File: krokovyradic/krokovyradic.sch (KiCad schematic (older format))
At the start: 1 part

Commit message: uprava
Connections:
- net labels added: +6V
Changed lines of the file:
@@
 LIBS:contrib
 LIBS:valves
+LIBS:krokovyradic-cache
 EELAYER 25 0
 EELAYER END
@@
 	1    0    0    -1
 $EndComp
+$Comp
+L +6V #PWR?
+U 1 1 5BD98FBB
+P 8000 3200
+F 0 "#PWR?" H 8000 3050 50  0001 C CNN
+F 1 "+6V" H 8000 3340 50  0000 C CNN
+F 2 "" H 8000 3200 50  0000 C CNN
+F 3 "" H 8000 3200 50  0000 C CNN
+	1    8000 3200
+	1    0    0    -1
+$EndComp

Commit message: arduino
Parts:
- removed IC?: ATMEGA328-A, TQFP32, symbol ATMEGA328-A
- added IC?: ATMEGA328-P, DIL28, symbol ATMEGA328-P
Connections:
- net labels removed: +6V
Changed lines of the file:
@@
 $EndDescr
 $Comp
-L ATMEGA328-A IC?
-U 1 1 5BD9900C
-P 5450 3600
-F 0 "IC?" H 4700 4850 50  0000 L BNN
-F 1 "ATMEGA328-A" H 5850 2200 50  0000 L BNN
-F 2 "TQFP32" H 5450 3600 50  0000 C CIN
-F 3 "" H 5450 3600 50  0000 C CNN
-	1    5450 3600
+L ATMEGA328-P IC?
+U 1 1 5BE2CED1
+P 4650 3400
+F 0 "IC?" H 3900 4650 50  0000 L BNN
+F 1 "ATMEGA328-P" H 5050 2000 50  0000 L BNN
+F 2 "DIL28" H 4650 3400 50  0000 C CIN
+F 3 "" H 4650 3400 50  0000 C CNN
+	1    4650 3400
 	1    0    0    -1
 $EndComp
-$Comp
-L +6V #PWR?
-U 1 1 5BD98FBB
-P 8000 3200
-F 0 "#PWR?" H 8000 3050 50  0001 C CNN
-F 1 "+6V" H 8000 3340 50  0000 C CNN
-F 2 "" H 8000 3200 50  0000 C CNN
-F 3 "" H 8000 3200 50  0000 C CNN
-	1    8000 3200
-	1    0    0    -1
-$EndComp

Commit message: uprava zapojeni
pridani soucastek
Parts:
- added A?: Pololu_Breakout_A4988, Module:Pololu_Breakout-16_15.2x20.3mm, symbol Driver_Motor:Pololu_Breakout_A4988
- added C?: C, symbol Device:C
- added M?: Stepper_Motor_bipolar, symbol Motor:Stepper_Motor_bipolar
- IC?: symbol ATMEGA328-P -> krokovyradic-rescue:ATMEGA328-P
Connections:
- net at IC?.22 (GND): now also A?.1 (GND)
- net at IC?.26 ((PCINT11/ADC3)PC3): now also A?.16 (DIR)
- net at IC?.27 ((PCINT12/SDA/ADC4)PC4): now also A?.15 (STEP)
- net at IC?.7 (VCC): now also A?.2 (VDD)
- new net: A?.13 (~RESET), A?.14 (~SLEEP)
- new net: A?.3 (1B), M?.2 (-)
- new net: A?.4 (1A), M?.1
- new net: A?.5 (2A), M?.3
- new net: A?.6 (2B), M?.4
- new net: A?.8 (VMOT), C?.1
- new net +7.5V: A?.7 (GND), C?.2
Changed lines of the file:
@@
-EESchema Schematic File Version 2
-LIBS:power
-LIBS:device
-LIBS:transistors
-LIBS:conn
-LIBS:linear
-LIBS:regul
-LIBS:74xx
-LIBS:cmos4000
-LIBS:adc-dac
-LIBS:memory
-LIBS:xilinx
-LIBS:microcontrollers
-LIBS:dsp
-LIBS:microchip
-LIBS:analog_switches
-LIBS:motorola
-LIBS:texas
-LIBS:intel
-LIBS:audio
-LIBS:interface
-LIBS:digital-audio
-LIBS:philips
-LIBS:display
-LIBS:cypress
-LIBS:siliconi
-LIBS:opto
-LIBS:atmel
-LIBS:contrib
-LIBS:valves
+EESchema Schematic File Version 4
 LIBS:krokovyradic-cache
-EELAYER 25 0
+EELAYER 26 0
 EELAYER END
 $Descr A4 11693 8268
@@
 $EndDescr
 $Comp
-L ATMEGA328-P IC?
+L Driver_Motor:Pololu_Breakout_A4988 A?
+U 1 1 5BE2F1A4
+P 7200 3300
+F 0 "A?" H 7250 4178 50  0000 C CNN
+F 1 "Pololu_Breakout_A4988" H 7250 4087 50  0000 C CNN
+F 2 "Module:Pololu_Breakout-16_15.2x20.3mm" H 7475 2550 50  0001 L CNN
+F 3 "https://www.pololu.com/product/2980/pictures" H 7300 3000 50  0001 C CNN
+	1    7200 3300
+	1    0    0    -1
+$EndComp
+$Comp
+L Motor:Stepper_Motor_bipolar M?
+U 1 1 5BE2F265
+P 8800 3450
+F 0 "M?" H 8988 3573 50  0000 L CNN
+F 1 "Stepper_Motor_bipolar" H 8988 3482 50  0000 L CNN
+F 2 "" H 8810 3440 50  0001 C CNN
+F 3 "http://www.infineon.com/dgdl/Application-Note-TLE8110EE_driving_UniPolarStepperMotor_V1.1.pdf?fileId=db3a30431be39b97011be5d0aa0a00b0" H 8810 3440 50  0001 C CNN
+	1    8800 3450
+	1    0    0    -1
+$EndComp
+$Comp
+L Device:C C?
+U 1 1 5BE2F449
+P 8650 4200
+F 0 "C?" H 8765 4246 50  0000 L CNN
+F 1 "C" H 8765 4155 50  0000 L CNN
+F 2 "" H 8688 4050 50  0001 C CNN
+F 3 "~" H 8650 4200 50  0001 C CNN
+	1    8650 4200
+	1    0    0    -1
+$EndComp
+Text GLabel 8950 4050 0    50   Input ~ 0
+47mF
+$Comp
+L power:+7.5V #PWR?
+U 1 1 5BE2F65F
+P 9650 4050
+F 0 "#PWR?" H 9650 3900 50  0001 C CNN
+F 1 "+7.5V" H 9665 4223 50  0000 C CNN
+F 2 "" H 9650 4050 50  0001 C CNN
+F 3 "" H 9650 4050 50  0001 C CNN
+	1    9650 4050
+	1    0    0    -1
+$EndComp
+$Comp
+L krokovyradic-rescue:ATMEGA328-P IC?
 U 1 1 5BE2CED1
 P 4650 3400
@@
 	1    0    0    -1
 $EndComp
+Wire Wire Line
+	7200 2600 6000 2600
+Wire Wire Line
+	6000 2600 6000 2100
+Wire Wire Line
+	4100 2100 4100 2050
+Wire Wire Line
+	4100 2050 3500 2050
+Wire Wire Line
+	3500 2050 3500 2300
+Wire Wire Line
+	3500 2300 3750 2300
+Wire Wire Line
+	4100 2100 6000 2100
+Wire Wire Line
+	7200 4100 5800 4100
+Wire Wire Line
+	5800 4100 5800 4900
+Wire Wire Line
+	5800 4900 3600 4900
+Wire Wire Line
+	3600 4900 3600 4500
+Wire Wire Line
+	3600 4500 3750 4500
+Wire Wire Line
+	5650 3550 6550 3550
+Wire Wire Line
+	6550 3550 6550 3300
+Wire Wire Line
+	6550 3300 6800 3300
+Wire Wire Line
+	5650 3450 6800 3450
+Wire Wire Line
+	6800 3450 6800 3400
+Wire Wire Line
+	6800 2900 6550 2900
+Wire Wire Line
+	6550 2900 6550 3000
+Wire Wire Line
+	6550 3000 6800 3000
+Wire Wire Line
+	7400 4100 8150 4100
+Wire Wire Line
+	8650 4350 9650 4350
+Wire Wire Line
+	9650 4350 9650 4050
+Connection ~ 8650 4350
+Wire Wire Line
+	8650 4050 8650 3950
+Wire Wire Line
+	8650 3950 9650 3950
+Wire Wire Line
+	8150 4100 8150 4350
+Wire Wire Line
+	8150 4350 8650 4350
+Wire Wire Line
+	7700 3200 8150 3200
+Wire Wire Line
+	8150 3200 8150 3000
+Wire Wire Line
+	8150 3000 8900 3000
+Wire Wire Line
+	8900 3000 8900 3150
+Wire Wire Line
+	7700 3300 8300 3300
+Wire Wire Line
+	8300 3300 8300 3050
+Wire Wire Line
+	8300 3050 8700 3050
+Wire Wire Line
+	8700 3050 8700 3150
+Wire Wire Line
+	7700 3400 8350 3400
+Wire Wire Line
+	8350 3400 8350 3350
+Wire Wire Line
+	8350 3350 8500 3350
+Wire Wire Line
+	7700 3500 8400 3500
+Wire Wire Line
+	8400 3500 8400 3550
+Wire Wire Line
+	8400 3550 8500 3550
+Wire Wire Line
+	7400 2600 10300 2600
+Wire Wire Line
+	10300 2600 10300 3800
+Wire Wire Line
+	10300 3800 8650 3800
+Wire Wire Line
+	8650 3800 8650 3950
+Connection ~ 8650 3950
 $EndSCHEMATC

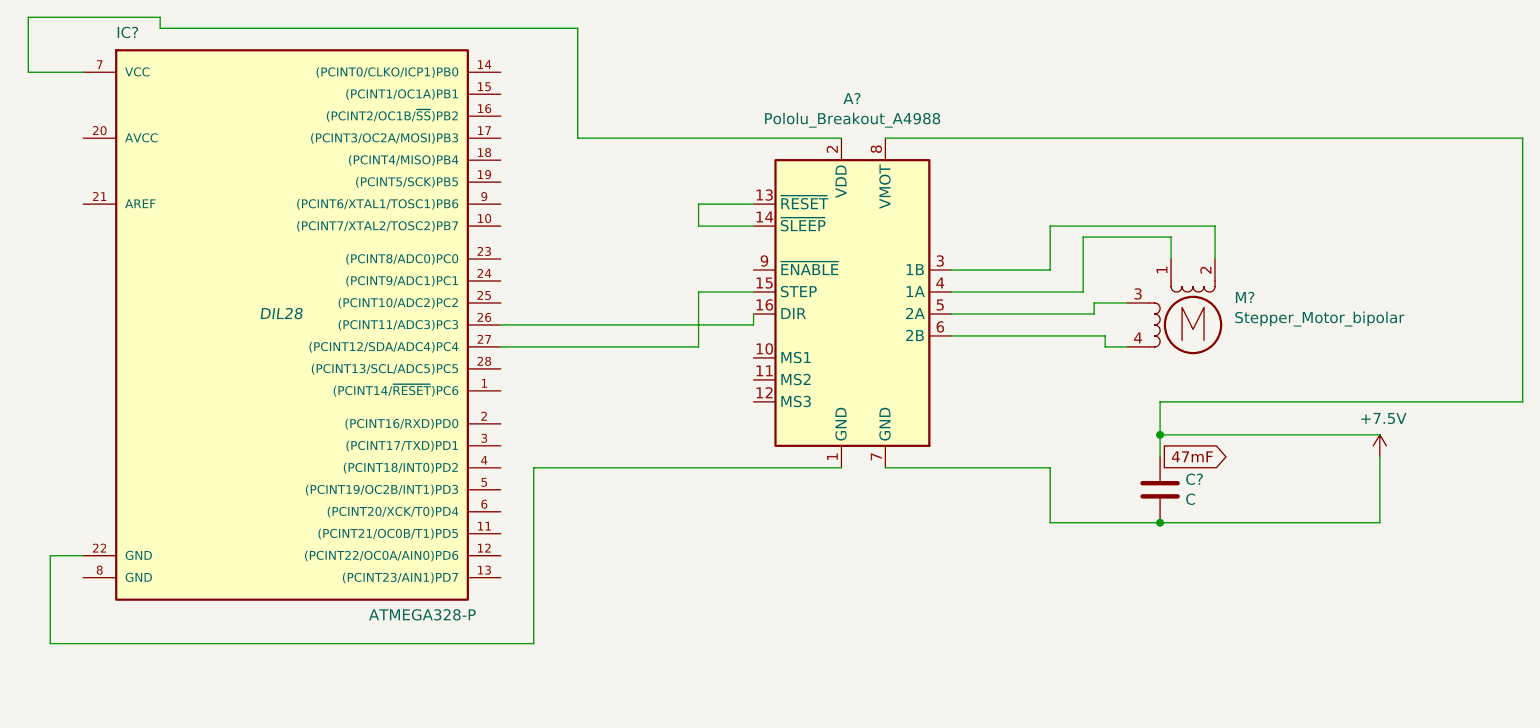
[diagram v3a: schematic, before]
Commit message: predelani pinu a laseru
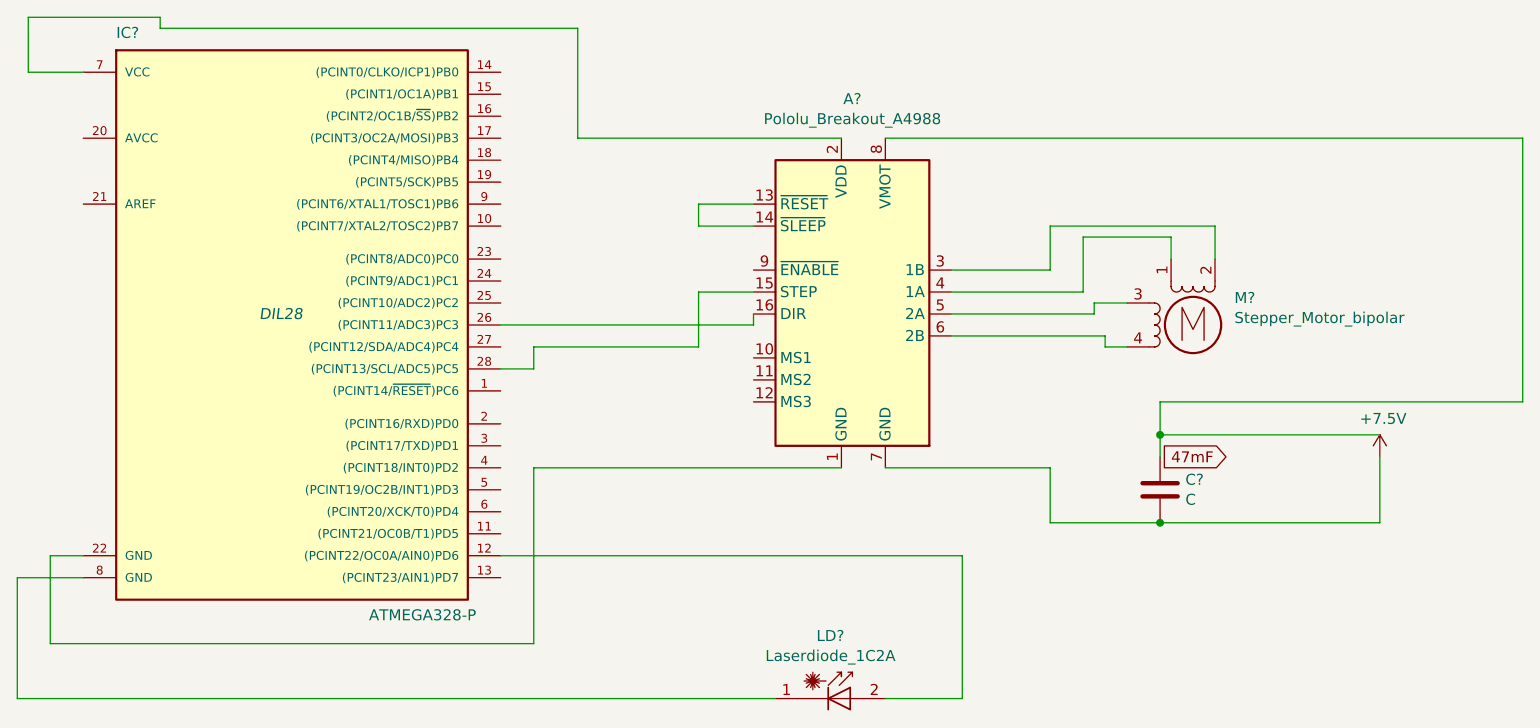
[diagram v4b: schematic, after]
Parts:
- added LD?: Laserdiode_1C2A, symbol Device:Laserdiode_1C2A
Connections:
- net at IC?.12 ((PCINT22/OC0A/AIN0)PD6): now also LD?.2 (A)
- net at IC?.27 ((PCINT12/SDA/ADC4)PC4): no longer A?.15 (STEP)
- net at IC?.28 ((PCINT13/SCL/ADC5)PC5): now also A?.15 (STEP)
- net at IC?.8 (GND): now also LD?.1 (K)
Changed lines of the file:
@@
 	3600 4500 3750 4500
-Wire Wire Line
-	5650 3550 6550 3550
 Wire Wire Line
 	6550 3550 6550 3300
@@
 	8650 3800 8650 3950
 Connection ~ 8650 3950
+Wire Wire Line
+	6550 3550 5800 3550
+Wire Wire Line
+	5800 3550 5800 3650
+Wire Wire Line
+	5800 3650 5650 3650
+$Comp
+L Device:Laserdiode_1C2A LD?
+U 1 1 5BEAAD8B
+P 7200 5150
+F 0 "LD?" H 7150 5435 50  0000 C CNN
+F 1 "Laserdiode_1C2A" H 7150 5344 50  0000 C CNN
+F 2 "" H 7100 5125 50  0001 C CNN
+F 3 "~" H 7230 4950 50  0001 C CNN
+	1    7200 5150
+	1    0    0    -1
+$EndComp
+Wire Wire Line
+	6900 5150 3450 5150
+Wire Wire Line
+	3450 5150 3450 4600
+Wire Wire Line
+	3450 4600 3750 4600
+Wire Wire Line
+	7400 5150 7750 5150
+Wire Wire Line
+	7750 5150 7750 4500
+Wire Wire Line
+	7750 4500 5650 4500
 $EndSCHEMATC
